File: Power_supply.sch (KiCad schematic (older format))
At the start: 16 parts

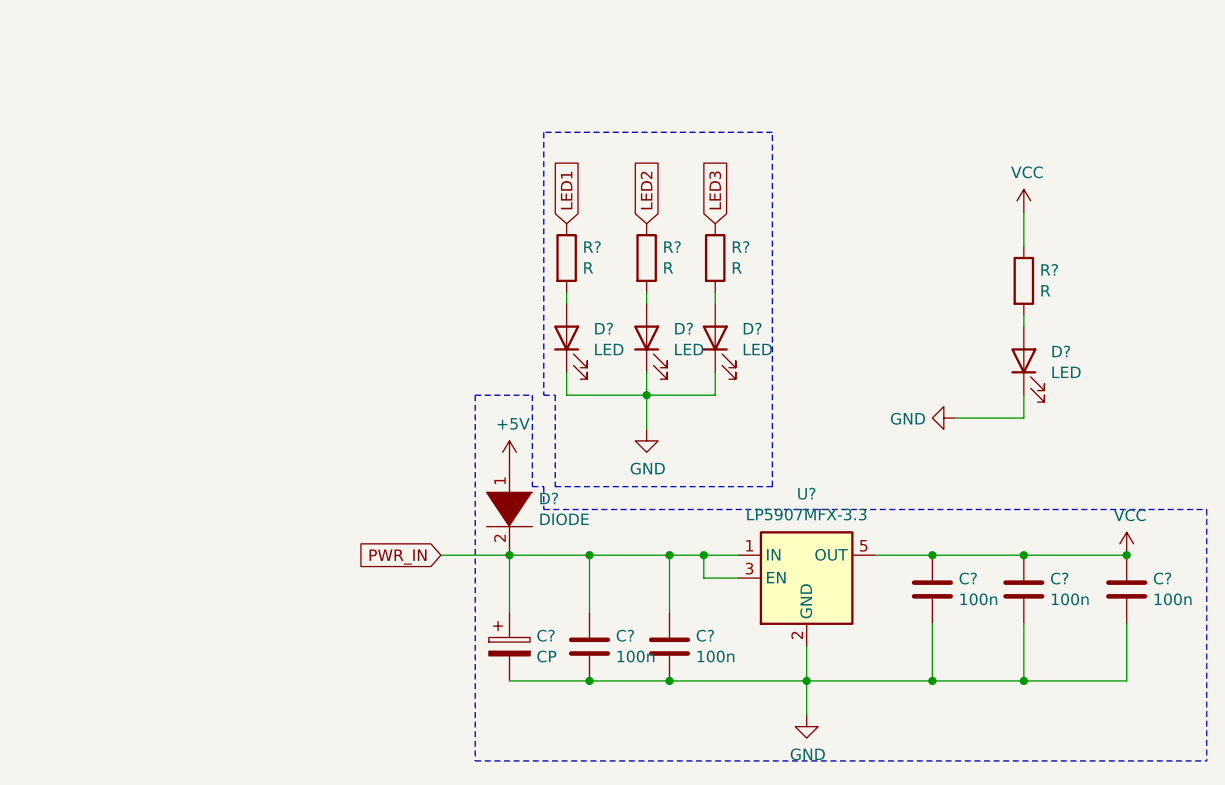
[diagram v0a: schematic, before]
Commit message: 4 layer add
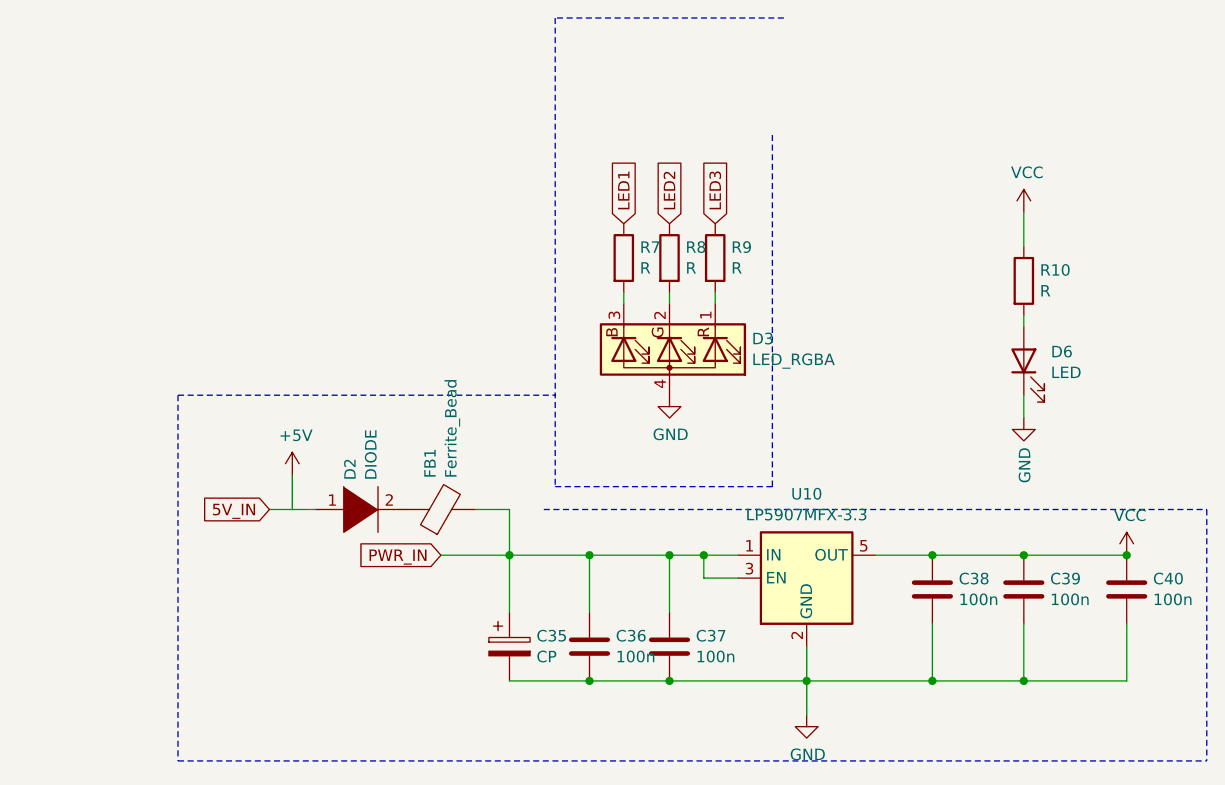
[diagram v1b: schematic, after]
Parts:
- removed D? (x3): LED, LED_SMD:LED_0603_1608Metric_Pad1.05x0.95mm_HandSolder, symbol Device:LED
- added D3: LED_RGBA, LED_SMD:LED_RGB_1210, symbol Device:LED_RGBA
- added FB1: Ferrite_Bead, Resistor_SMD:R_0805_2012Metric, symbol Device:Ferrite_Bead
- gave numbers to parts that had none: 13
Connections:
- net GND: now also D3.4 (A)
- net PWR_IN: now also FB1.2; no longer D2.2 (A)
- net at R7.2: now also D3.3 (BK)
- net at R8.2: now also D3.2 (GK)
- net at R9.2: now also D3.1 (RK)
- new net: D2.2 (A), FB1.1
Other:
- moved on the sheet: D2, R7, R8

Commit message: finish board
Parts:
- added J19: Conn_01x02_Male, Connector_PinHeader_2.54mm:PinHeader_1x02_P2.54mm_Vertical, symbol Connector:Conn_01x02_Male
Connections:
- net +5V: now also J19.1 (Pin_1)
- net GND: now also J19.2 (Pin_2)
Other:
- moved on the sheet: D2
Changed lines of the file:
@@
 Connection ~ 4150 4200
-$Comp
-L pspice:DIODE D?
-U 1 1 5F5FCF99
-P 3500 4000
-AR Path="/5F5FCF99" Ref="D?"  Part="1"
-AR Path="/5F569749/5F5FCF99" Ref="D?"  Part="1"
-AR Path="/5F5EB1A4/5F5FCF99" Ref="D2"  Part="1"
-AR Path="/5F6068B8/5F5FCF99" Ref="D?"  Part="1"
-F 0 "D2" V 3454 4128 50  0000 L CNN
-F 1 "DIODE" V 3545 4128 50  0000 L CNN
-F 2 "Diode_SMD:D_1206_3216Metric" H 3500 4000 50  0001 C CNN
-F 3 "~" H 3500 4000 50  0001 C CNN
-	1    3500 4000
-	1    0    0    -1
-$EndComp
 $Comp
 L power:+5V #PWR?
 U 1 1 5F5FCF9F
-P 3200 3850
+P 2750 3850
 AR Path="/5F5FCF9F" Ref="#PWR?"  Part="1"
 AR Path="/5F569749/5F5FCF9F" Ref="#PWR?"  Part="1"
 AR Path="/5F5EB1A4/5F5FCF9F" Ref="#PWR0174"  Part="1"
 AR Path="/5F6068B8/5F5FCF9F" Ref="#PWR?"  Part="1"
-F 0 "#PWR0174" H 3200 3700 50  0001 C CNN
-F 1 "+5V" H 3215 4023 50  0000 C CNN
-F 2 "" H 3200 3850 50  0001 C CNN
-F 3 "" H 3200 3850 50  0001 C CNN
-	1    3200 3850
+F 0 "#PWR0174" H 2750 3700 50  0001 C CNN
+F 1 "+5V" H 2765 4023 50  0000 C CNN
+F 2 "" H 2750 3850 50  0001 C CNN
+F 3 "" H 2750 3850 50  0001 C CNN
+	1    2750 3850
 	1    0    0    -1
 $EndComp
@@
 Wire Wire Line
 	6400 2850 6400 2700
-Text GLabel 3850 4200 0    50   Input ~ 0
+Text GLabel 4100 3700 1    50   Input ~ 0
 PWR_IN
 Wire Wire Line
-	3850 4200 4150 4200
+	4100 3700 4100 4000
 Wire Notes Line
 	7200 4000 7200 5100
 Wire Notes Line
-	2700 3500 2700 5100
+	2000 3500 2000 5100
 Wire Wire Line
 	4150 4200 4500 4200
@@
 	4150 4200 4150 4000
 Wire Wire Line
-	4150 4000 4000 4000
+	4150 4000 4100 4000
 $Comp
 L Device:Ferrite_Bead FB1
@@
 	2700 5100 7200 5100
 Wire Wire Line
-	3300 4000 3200 4000
-Wire Wire Line
-	3200 4000 3200 3850
+	2750 4000 2750 3850
 $Comp
 L Device:LED_RGBA D3
@@
 $EndComp
 Wire Wire Line
-	3200 4000 3100 4000
-Text GLabel 3100 4000 0    50   Input ~ 0
-5V_IN
+	2950 4100 2950 4150
+Wire Wire Line
+	2750 4100 2950 4100
+$Comp
+L power:GND #PWR?
+U 1 1 5F592851
+P 2950 4150
+AR Path="/5F592851" Ref="#PWR?"  Part="1"
+AR Path="/5F41B667/5F592851" Ref="#PWR?"  Part="1"
+AR Path="/5F5517E4/5F592851" Ref="#PWR?"  Part="1"
+AR Path="/5F5C31DE/5F592851" Ref="#PWR?"  Part="1"
+AR Path="/5F5EB1A4/5F592851" Ref="#PWR0155"  Part="1"
+F 0 "#PWR0155" H 2950 3900 50  0001 C CNN
+F 1 "GND" H 2955 3977 50  0000 C CNN
+F 2 "" H 2950 4150 50  0001 C CNN
+F 3 "" H 2950 4150 50  0001 C CNN
+	1    2950 4150
+	1    0    0    -1
+$EndComp
+$Comp
+L Connector:Conn_01x02_Male J?
+U 1 1 5F592857
+P 2550 4000
+AR Path="/5F592857" Ref="J?"  Part="1"
+AR Path="/5F41B667/5F592857" Ref="J?"  Part="1"
+AR Path="/5F5517E4/5F592857" Ref="J?"  Part="1"
+AR Path="/5F5C31DE/5F592857" Ref="J?"  Part="1"
+AR Path="/5F5EB1A4/5F592857" Ref="J19"  Part="1"
+F 0 "J19" H 2658 4181 50  0000 C CNN
+F 1 "Conn_01x02_Male" H 2658 4090 50  0000 C CNN
+F 2 "Connector_PinHeader_2.54mm:PinHeader_1x02_P2.54mm_Vertical" H 2550 4000 50  0001 C CNN
+F 3 "~" H 2550 4000 50  0001 C CNN
+	1    2550 4000
+	1    0    0    -1
+$EndComp
+Wire Wire Line
+	2750 4000 2800 4000
+$Comp
+L pspice:DIODE D?
+U 1 1 5F5FCF99
+P 3000 4000
+AR Path="/5F5FCF99" Ref="D?"  Part="1"
+AR Path="/5F569749/5F5FCF99" Ref="D?"  Part="1"
+AR Path="/5F5EB1A4/5F5FCF99" Ref="D2"  Part="1"
+AR Path="/5F6068B8/5F5FCF99" Ref="D?"  Part="1"
+F 0 "D2" V 2954 4128 50  0000 L CNN
+F 1 "DIODE" V 3045 4128 50  0000 L CNN
+F 2 "Diode_SMD:D_1206_3216Metric" H 3000 4000 50  0001 C CNN
+F 3 "~" H 3000 4000 50  0001 C CNN
+	1    3000 4000
+	1    0    0    -1
+$EndComp
+Connection ~ 4100 4000
+Wire Wire Line
+	4100 4000 4000 4000
+Connection ~ 2750 4000
+Wire Wire Line
+	3200 4000 3700 4000
 $EndSCHEMATC
